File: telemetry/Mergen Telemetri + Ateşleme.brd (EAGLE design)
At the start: 53.6 x 90.7 mm, 78 parts, among them J2 U.FL, Q2 IRLML6344TRPBF, Q3 IRLML6344TRPBF, U1 STM32F401CCU6UFQFPN-48_7X7X0P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, U2 ADXL345BCCZ, U3 LPS22HB, U4 L86, U6 AMS1117-3.3, U7 AMS1117-3.3, Y1 ABM3B-26.000MHZ-10-1-U-T

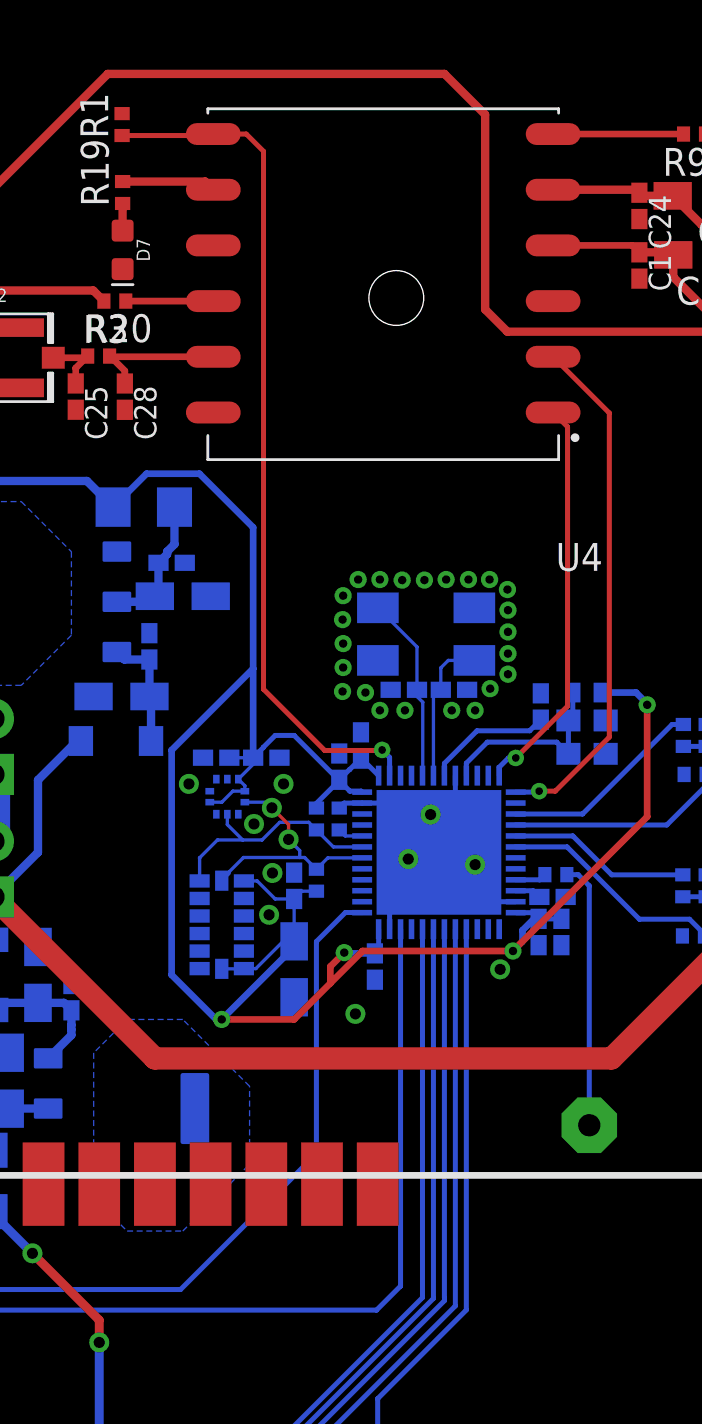
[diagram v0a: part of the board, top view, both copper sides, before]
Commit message: Some modification was maken on the LPS22HB and ADXL345
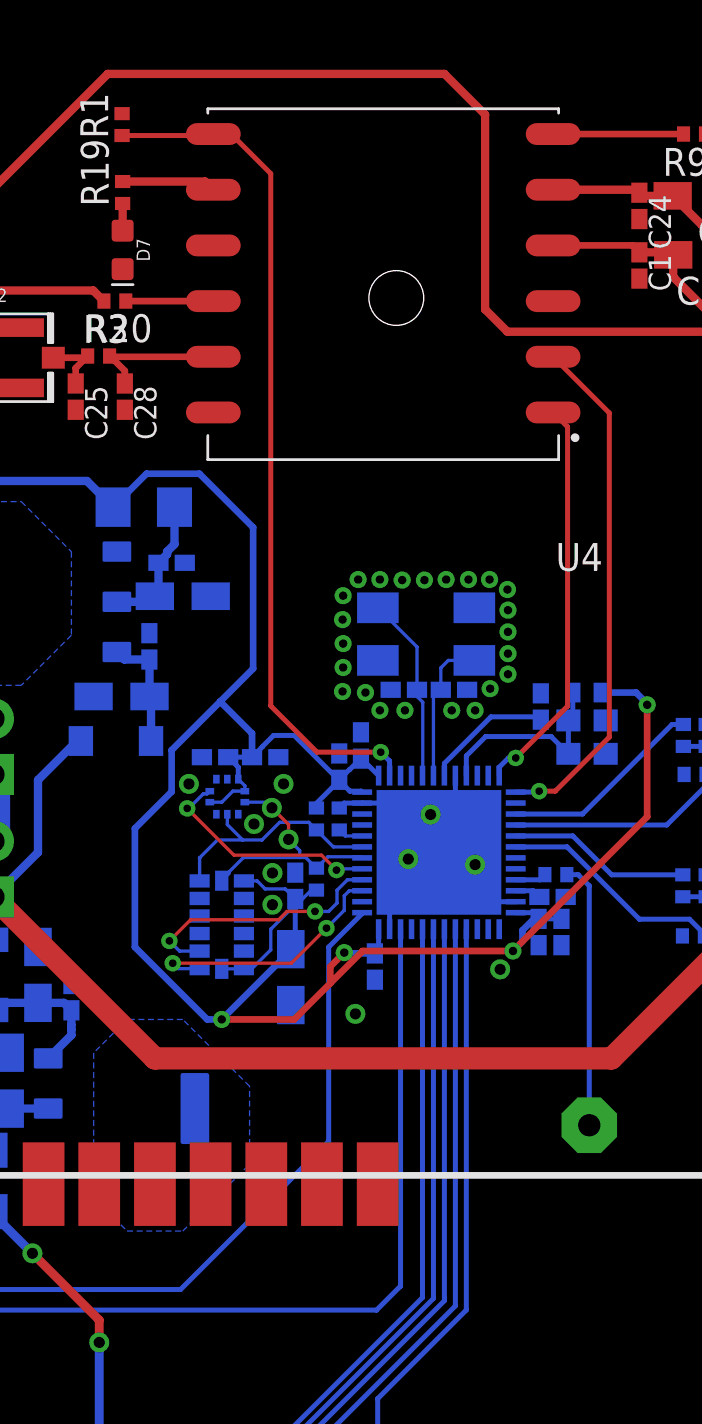
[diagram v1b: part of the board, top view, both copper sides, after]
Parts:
- C12: value 0.1uF -> 4.7uF
- C13: value 1uF -> 10uF
- moved C14 2.34 mm to (18.0, 49.6), turned to 0 degrees
- moved C12 2.24 mm to (20.3, 49.6), turned to 180 degrees
- moved C13 0.39 mm to (21.4, 39.5)
- moved R5 0.05 mm to (22.6, 44.0)
- moved C11 0.05 mm to (21.6, 43.7)
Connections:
- new net INT: U1.41, U3.7
- new net INT1: U1.39, U2.8
- new net INT2: U1.40, U2.9
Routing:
- net INT2: track 0.00 -> 11.9 mm, vias 0 -> 2
- net INT1: track 0.00 -> 11.7 mm, vias 0 -> 2
- net INT: track 0.00 -> 10.5 mm, vias 0 -> 2
- net 3.3V: track 246.5 -> 248.4 mm

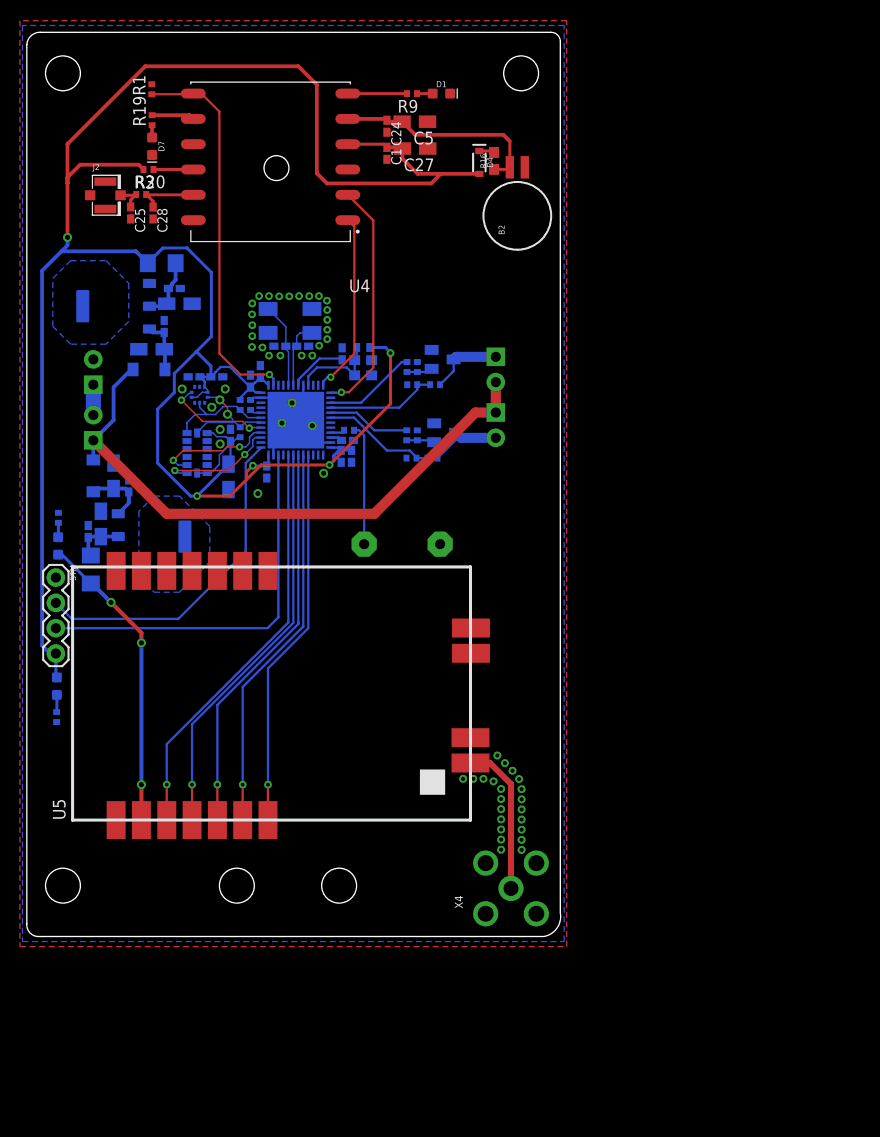
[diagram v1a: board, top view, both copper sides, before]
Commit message: Routes were be extended
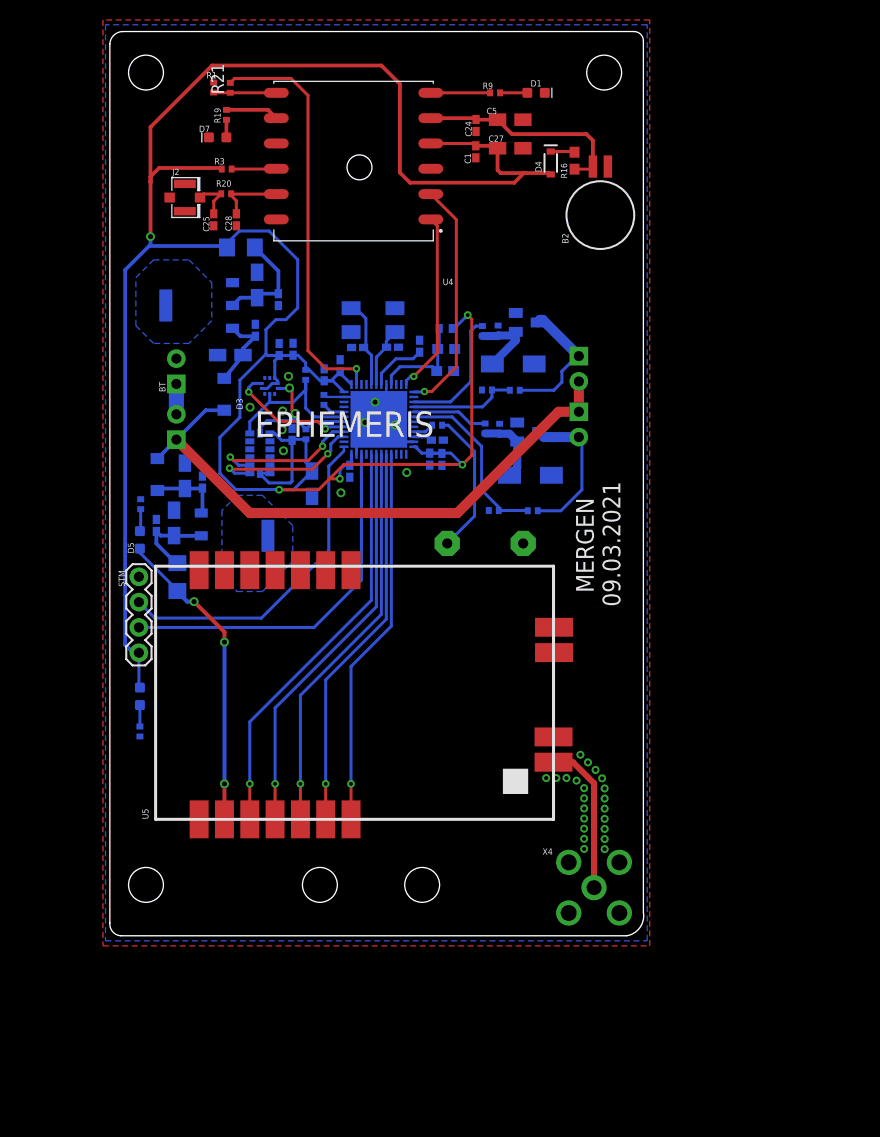
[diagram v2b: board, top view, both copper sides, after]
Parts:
- added ESDA, ESDA1: 12V, Wurth_EMC Components_WE-TVSP:WE-TVSP_DO-214AC_UNIDIRECTIONAL
- added R21: 680, rcl:R0402
- moved R7 11.4 mm to (52.0, 36.1)
- moved C9 10.5 mm to (26.4, 57.3), turned to 270 degrees
- moved R8 9.79 mm to (48.1, 36.1)
- moved C5 9.58 mm to (49.7, 75.4)
- moved C27 9.55 mm to (49.7, 72.5)
- moved D1 9.50 mm to (52.3, 78.1)
- moved Q3 9.21 mm to (51.4, 55.0)
- moved C8 9.15 mm to (24.1, 54.2)
- moved C22 9.07 mm to (42.8, 41.3)
- moved C20 9.02 mm to (37.9, 52.5)
- moved C18 9.02 mm to (42.4, 43.2)
- moved C14 8.96 mm to (26.5, 52.3), turned to 90 degrees
- moved C24 8.94 mm to (46.3, 74.8)
- moved C1 8.92 mm to (46.3, 72.1)
- moved C21 8.89 mm to (41.6, 41.3)
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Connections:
- new net N$20: R1.1, R21.1, U4.7
- net FN: now also R21.2; no longer R1.1, U4.7
- net GND: now also ESDA.2, ESDA1.2
- net N$13: now also ESDA.1
- net N$6: now also ESDA1.1
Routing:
- net 3.3V: track 248.4 -> 267.7 mm
- net MAIN: track 7.50 -> 14.9 mm
- net MAIN_S: track 11.4 -> 18.1 mm
- net N$20: track 0.00 -> 6.31 mm
- net APG: track 7.45 -> 13.7 mm
- net SDA: track 11.1 -> 17.0 mm
- net N$6: track 2.61 -> 7.70 mm
- net N$5: track 6.27 -> 10.7 mm
- net N$13: track 2.84 -> 7.26 mm
- net N$4: track 4.96 -> 8.83 mm
- net INT1: track 11.7 -> 15.5 mm
- net APG_F: track 9.34 -> 13.0 mm
- net SCL: track 11.5 -> 15.0 mm
- net INT2: track 11.9 -> 15.3 mm
- net N$2: track 5.37 -> 8.05 mm
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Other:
- board text added: "EPHEMERIS"
- board text added: "MERGEN 09.03.2021"

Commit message: LOGO was uploaded
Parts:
- moved VDDA2 0.84 mm to (42.3, 50.1)
- moved SG1 0.56 mm to (47.8, 32.9)
- moved C15 0.33 mm to (32.8, 50.4)
- moved C22 0.31 mm to (42.5, 41.4)
- moved C21 0.28 mm to (41.4, 41.4)
- moved C16 0.24 mm to (31.3, 49.7)

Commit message: Extra polygon was added for methal distance and 1x4 JST connector was added for payload
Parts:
- added C26, C29: 1000uF, adafruit:150CLZ-1010
- added J1: (no value), SparkFun-Connectors:JST-4-PTH-VERT
- moved MN 28.0 mm to (78.9, 29.0)
- moved APG 27.8 mm to (78.9, 35.0)
- moved C6 27.6 mm to (37.4, 17.4)
- moved D2 27.6 mm to (35.7, 22.3)
- moved C2 27.4 mm to (38.2, 22.2)
- moved D4 27.2 mm to (74.9, 53.9)
- moved VDDA1 27.2 mm to (64.4, 35.2)
- moved C11 27.2 mm to (48.9, 26.6)
- moved C16 27.2 mm to (52.3, 32.5)
- moved C24 27.2 mm to (67.4, 57.6)
- moved C28 27.2 mm to (43.3, 48.2)
- moved D5 27.2 mm to (33.6, 16.1)
- moved D6 27.2 mm to (33.6, 0.36)
- moved R17 27.2 mm to (33.6, -3.17)
- moved R18 27.2 mm to (33.7, 19.6)
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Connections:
- new net 6RX: J1.3, U1.33
- new net 6TX: J1.2, U1.32
- net 5V: now also C26.+, C29.+
- net AUX: now also U1.27; no longer U1.32
- net GND: now also C26.-, C29.-, J1.1
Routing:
- net 6RX: track 0.00 -> 43.5 mm, vias 0 -> 1
- net 6TX: track 0.00 -> 41.0 mm, vias 0 -> 1
- net AUX: track 41.7 -> 47.9 mm
- net 5V: track 31.1 -> 36.6 mm
- net APG: track 13.7 -> 16.2 mm
- net VCC: track 59.2 -> 61.0 mm
- net MAIN: track 14.9 -> 16.4 mm
- net 3.3V: track 267.2 -> 267.8 mm
- added copper zone on layer 1, net D
- added copper zone on layer 16, net D
